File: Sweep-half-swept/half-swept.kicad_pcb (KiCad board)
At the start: 2 copper layers, 109 x 86.9 mm, 26 parts, among them J2 AudioJack4dpb, SW10 SW_Push, SW11 SW_Push, SW12 SW_Push, SW14 SW_Push, SW15 SW_Push, SW16 SW_Push, SW17 SW_Push, SW18 SW_Push, SW2 SW_Push, SW2 SW_SPDT, SW20 SW_Push, SW21 SW_Push, SW3 SW_Push, SW4 SW_Push, SW5 SW_Push, SW6 SW_Push, SW8 SW_Push, SW9 SW_Push, U1 ProMicro-kbd

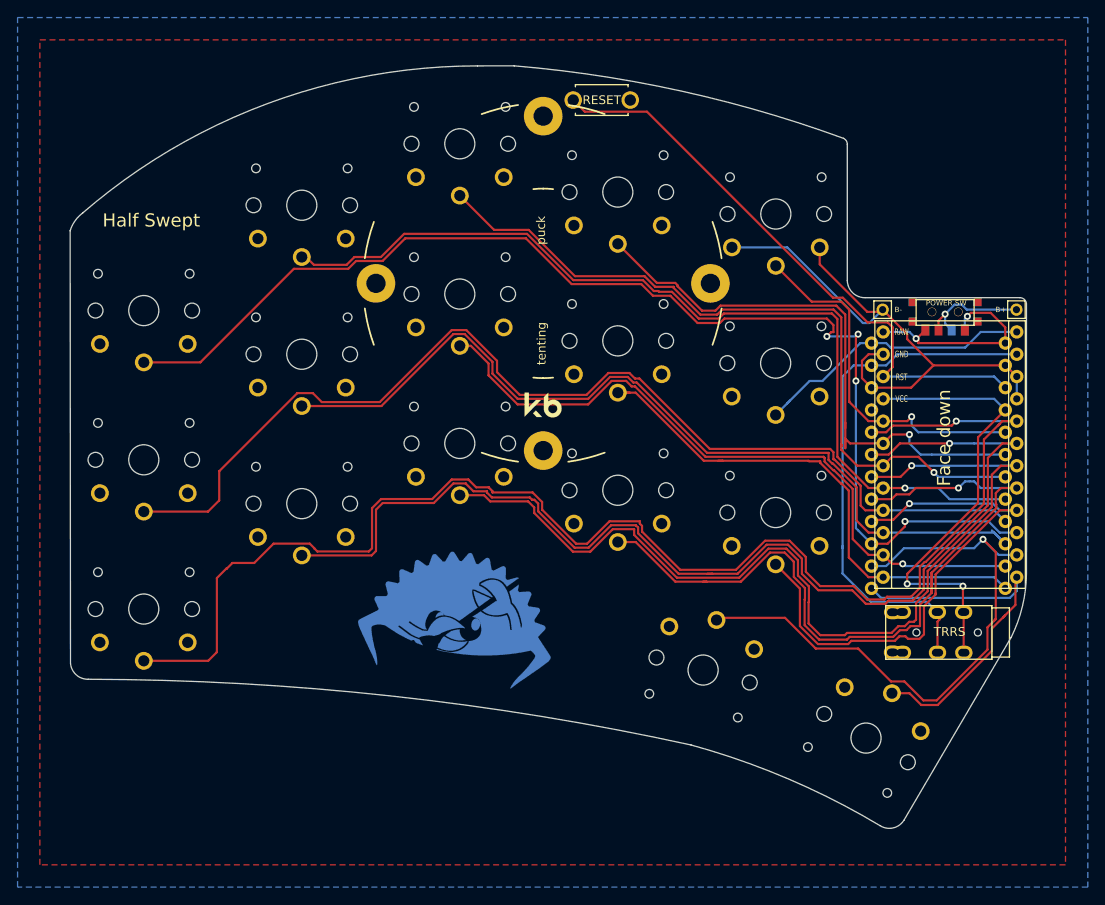
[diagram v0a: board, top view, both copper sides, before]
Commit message: removed holes + added footprints
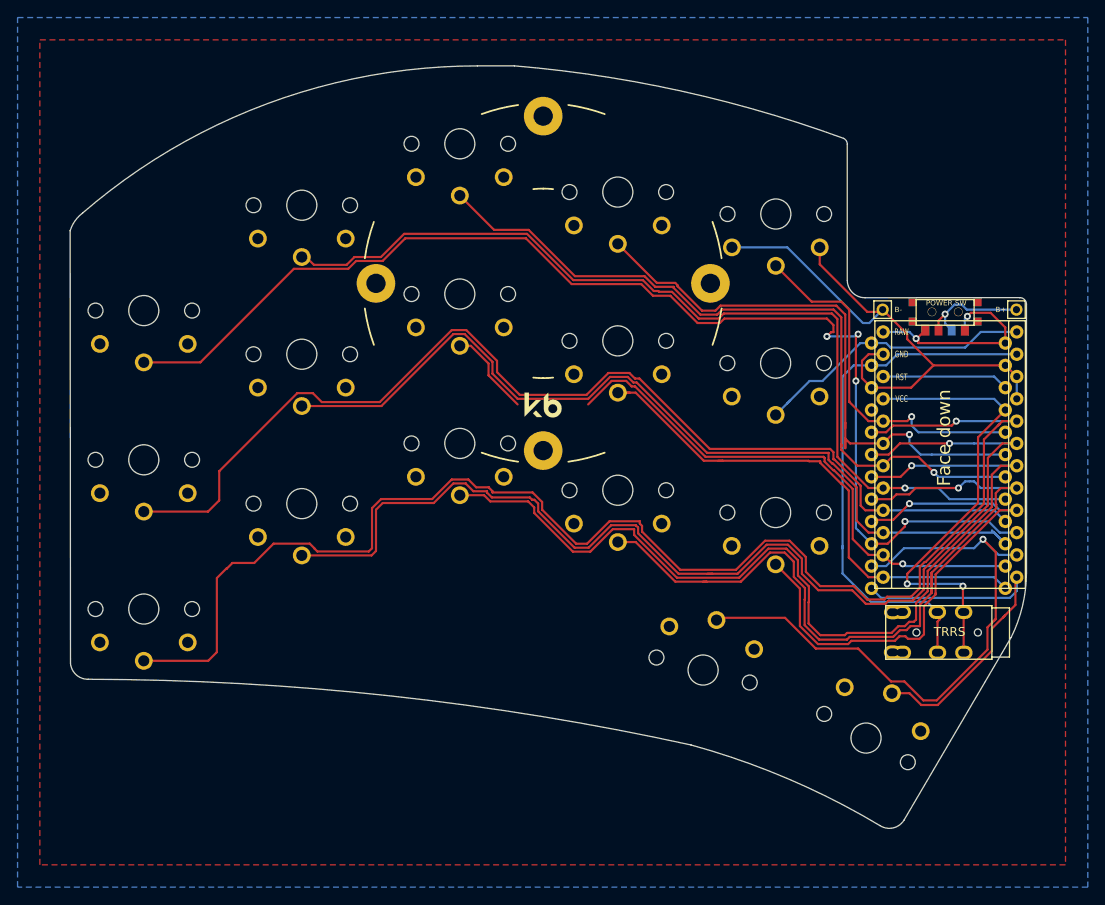
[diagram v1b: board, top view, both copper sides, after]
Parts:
- removed G***: LOGO, Kailh:ferris_broom
- removed RSW1: SW_Push, kbd:ResetSW
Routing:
- net reset: track 68.1 -> 14.9 mm
- net Switch8: track 79.2 -> 71.2 mm
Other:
- net class Default removed
- board text removed: "Half Swept"
